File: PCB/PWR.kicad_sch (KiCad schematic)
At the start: 8 parts, among them U1 STPMIC1APQR

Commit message: PCB_Update
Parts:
- removed C1: 4.7uF, Capacitor_SMD:C_0402_1005Metric, symbol Device:C
- added C10, C11, C12, C13, C14, C15, C17: 10uF, Capacitor_SMD:C_0603_1608Metric, symbol Device:C
- added C16, C8, C9: 1uF, Capacitor_SMD:C_0402_1005Metric, symbol Device:C
- added C18: 4.7uF, Capacitor_SMD:C_0603_1608Metric, symbol Device:C
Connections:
- net at U1.12 (BUCK2IN): now also C11.2
- net at U1.13 (LDO3IN): now also C14.2
- net at U1.14 (LDO3OUT): now also C15.1
- net at U1.16 (VREFDDR): now also C16.1
- net at U1.19 (LDO25IN): now also C9.2
- net at U1.22 (LDO16IN): now also C8.2
- net at U1.24 (BUCK4IN): now also C13.2
- net at U1.28 (BUCK3IN): now also C12.2
- net at U1.35 (VBUSOTG): now also C18.1
- net at U1.8 (BUCK1IN): now also C10.2
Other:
- note removed: "CVIN, CLDO1OUT, CLDO2OUT, CLDO4OUT, CLDO5OUT, CLDO6OUT, CINTLDO"
- moved on the sheet: C2, C3, C4, C5, C6, C7, U1

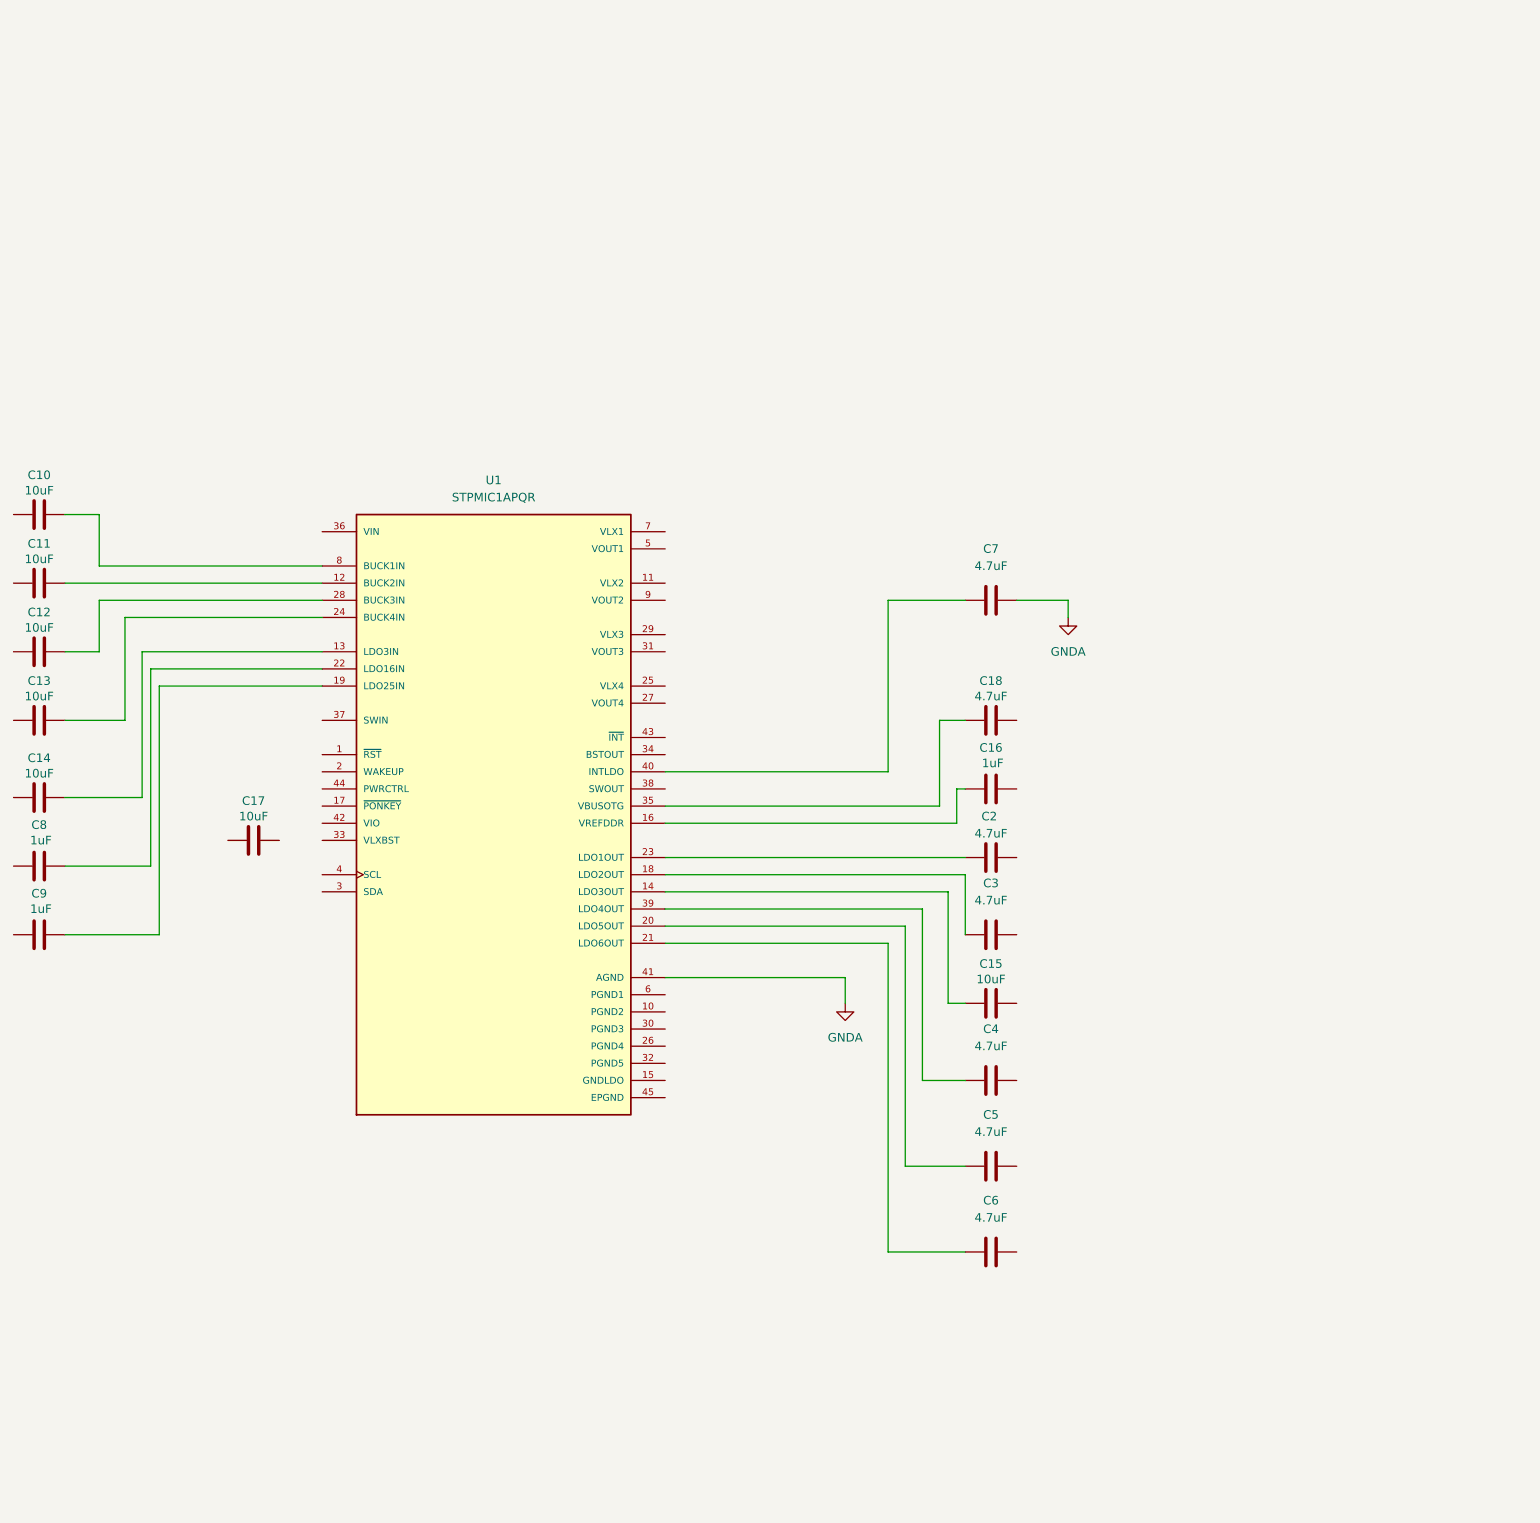
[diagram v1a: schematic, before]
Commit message: PCB_UPDATE. PWR DONE, DDR STARTED
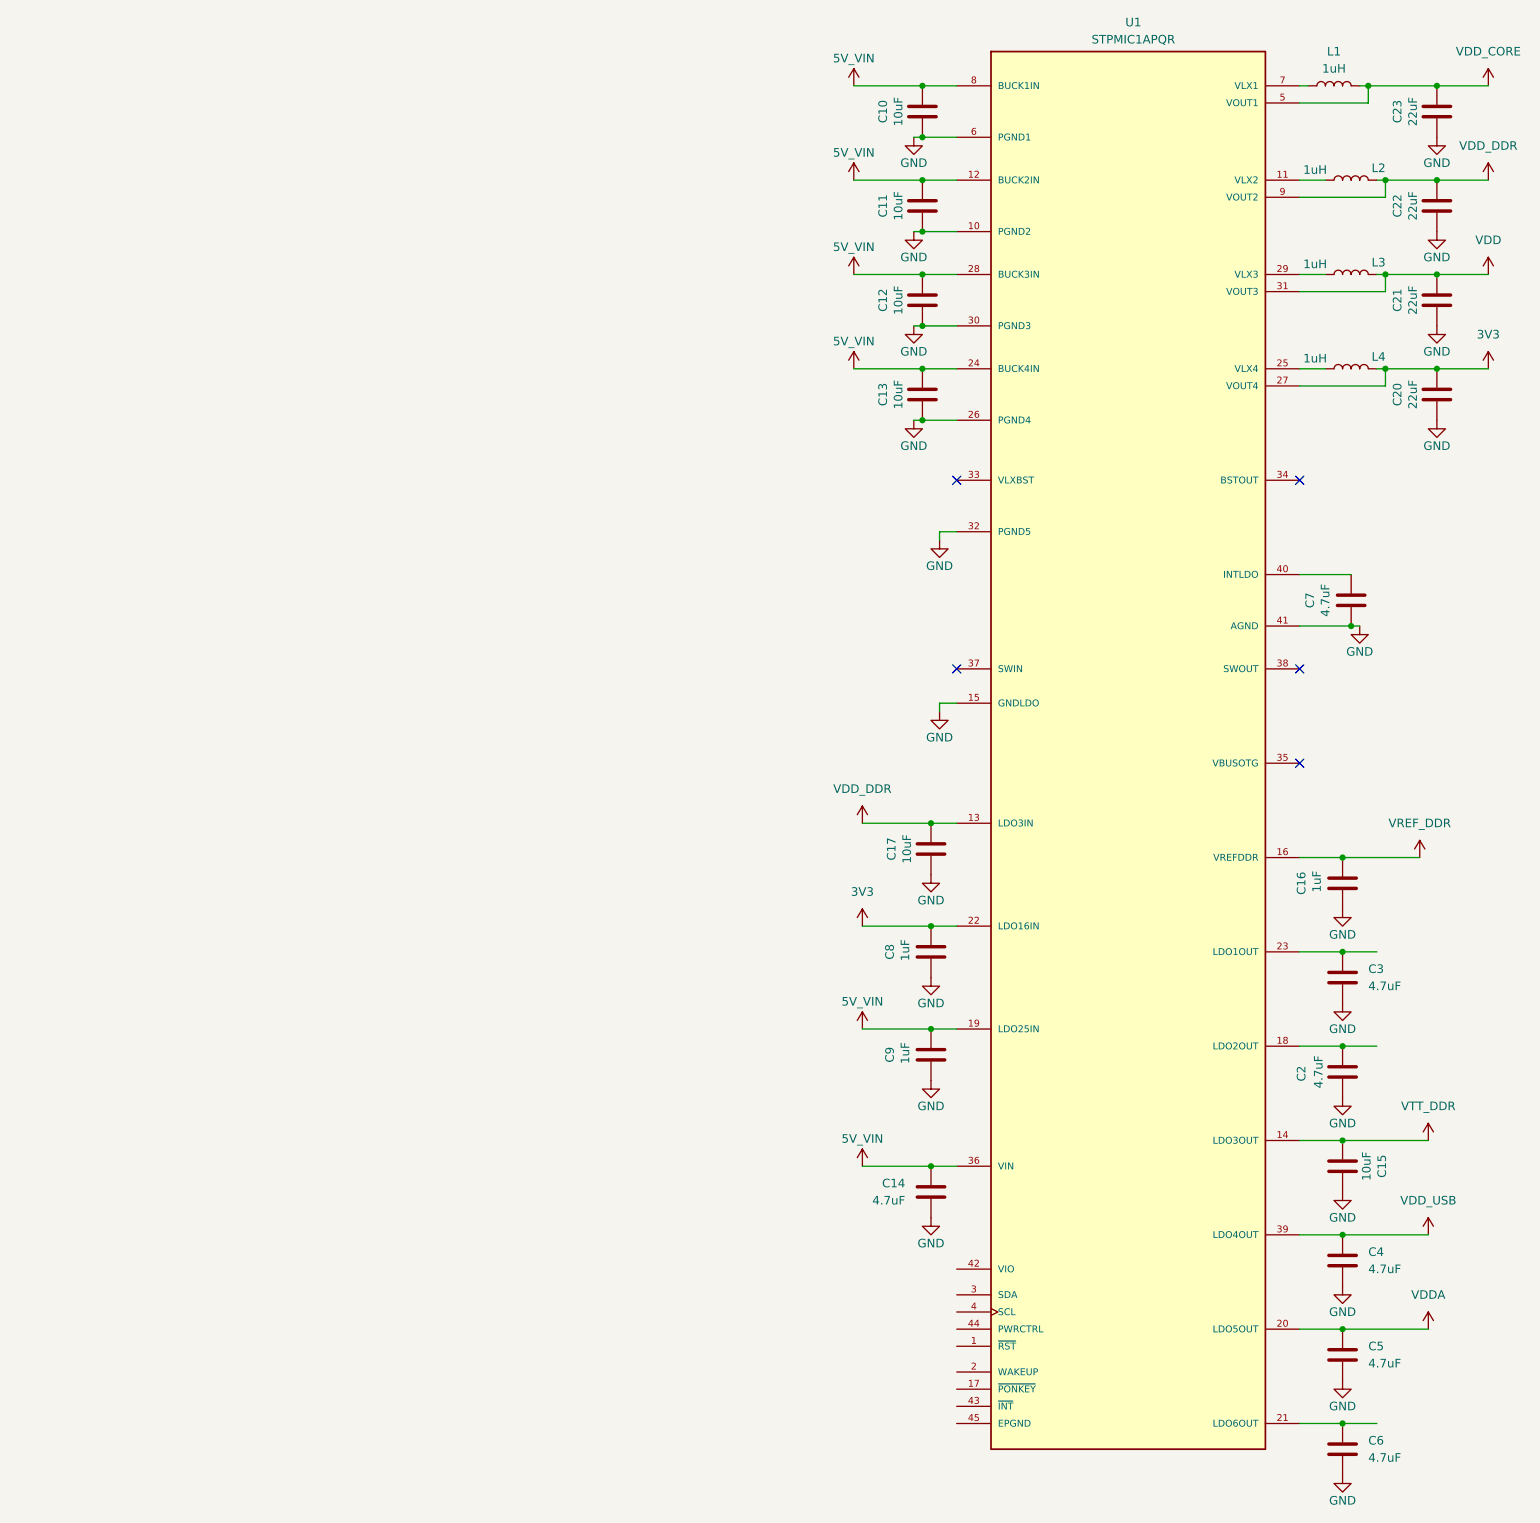
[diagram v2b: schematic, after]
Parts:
- removed C18: 4.7uF, Capacitor_SMD:C_0603_1608Metric, symbol Device:C
- added C20, C21, C22, C23: 22uF, Capacitor_SMD:C_0603_1608Metric, symbol Device:C
- added L1, L2, L3, L4: 1uH, Inductor_SMD:L_1008_2520Metric, symbol Device:L
- C14: value 10uF -> 4.7uF; footprint Capacitor_SMD:C_0603_1608Metric -> Capacitor_SMD:C_0402_1005Metric; Mouser P/N 81-GRT188R61A106KE3D -> 81-GRM155R60J475ME7J; P/N GRT188R61A106KE13D -> GRM155R60J475ME47
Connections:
- net GND: now reaches C11.1
- net GND: now also C10.1, C12.1, C13.1, C14.1, C15.2, C16.1, C17.1, C2.1, C3.1, C4.1, C5.1, C6.1, C7.1, C8.1, C9.1, U1.10 (PGND2), U1.15 (GNDLDO), U1.26 (PGND4), U1.30 (PGND3), U1.32 (PGND5), U1.41 (AGND), U1.6 (PGND1), C20.1, C21.1, C22.1, C23.1
- net 5V_VIN: now reaches C11.2, U1.12 (BUCK2IN)
- net 5V_VIN: now also C10.2, C12.2, C13.2, C14.2, C9.2, U1.19 (LDO25IN), U1.24 (BUCK4IN), U1.28 (BUCK3IN), U1.36 (VIN), U1.8 (BUCK1IN)
- net at U1.11 (VLX2): now also L2.1
- net VDD_DDR: now reaches U1.13 (LDO3IN)
- net VDD_DDR: now also C17.2, U1.9 (VOUT2), C22.2, L2.2; no longer C14.2
- net VTT_DDR: now reaches C15.1, U1.14 (LDO3OUT)
- net VREF_DDR: now reaches U1.16 (VREFDDR)
- net VREF_DDR: now also C16.2; no longer C16.1
- net at U1.18 (LDO2OUT): now also C2.2; no longer C3.1
- net VDDA: now reaches U1.20 (LDO5OUT)
- net VDDA: now also C5.2; no longer C5.1
- net at U1.21 (LDO6OUT): now also C6.2; no longer C6.1
- net 3V3: now reaches C8.2, U1.22 (LDO16IN)
- net 3V3: now also U1.27 (VOUT4), C20.2, L4.2
- net at U1.23 (LDO1OUT): now also C3.2; no longer C2.1
- net at U1.25 (VLX4): now also L4.1
- net at U1.29 (VLX3): now also L3.1
- net VDD: now reaches U1.31 (VOUT3)
- net VDD: now also C21.2, L3.2
- net VDD_USB: now reaches U1.39 (LDO4OUT)
- net VDD_USB: now also C4.2; no longer C4.1
- net at U1.40 (INTLDO): now also C7.2; no longer C7.1
- net VDD_CORE: now reaches U1.5 (VOUT1)
- net VDD_CORE: now also C23.2, L1.2
- net at U1.7 (VLX1): now also L1.1
- removed net GNDA: C7.2, U1.41 (AGND)
- no-connect marks 0 -> 5
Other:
- moved on the sheet: C10, C11, C12, C13, C15, C16, C17, C2, C3, C4, C5, C6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

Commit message: PCB_UPDATE
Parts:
- added R40: 0, symbol Device:R
- U1: Availability In Stock -> (none); Check_prices https://www.snapeda.com/parts/STPMIC1APQR/STMicroelectronic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 -> (none); Description_1 General Purpose PMIC 44-WFQFN (5x6) -> (none); MANUFACTURER STMicroelectronics -> (none); MAXIMUM_PACKAGE_HEIGHT 0.8mm -> (none); MF STMicroelectronics -> (none); MP STPMIC1APQR -> (none); Mouser P/N (none) -> 511-STPMIC1APQR; P/N (none) -> STPMIC1APQR; PARTREV 8 -> (none); Package WFQFN-44 STMicroelectronics -> (none); Price None -> (none); STANDARD IPC 7351B -> (none); SnapEDA_Link https://www.snapeda.com/parts/STPMIC1APQR/STMicroelectronic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 -> (none)
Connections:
- net at U1.1 (~{RST}): now also R40.1
- net PWR_ON: now reaches U1.44 (PWRCTRL)
- new net NRST: R40.2
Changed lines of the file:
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@@
 	(wire
 		(pts
+			(xy 280.67 222.25) (xy 285.75 222.25)
+		)
+		(stroke
+			(width 0)
+			(type default)
+		)
+	)
+	(wire
+		(pts
 			(xy 303.53 85.09) (xy 304.8 85.09)
 		)
@@
 	(wire
 		(pts
+			(xy 293.37 222.25) (xy 309.88 222.25)
+		)
+		(stroke
+			(width 0)
+			(type default)
+		)
+	)
+	(wire
+		(pts
 			(xy 373.38 77.47) (xy 373.38 80.01)
 		)
@@
 		)
 	)
+	(global_label "NRST"
+		(shape input)
+		(at 280.67 222.25 180)
+		(fields_autoplaced yes)
+		(effects
+			(font
+				(size 1.27 1.27)
+			)
+			(justify right)
+		)
+		(property "Intersheetrefs" "${INTERSHEET_REFS}"
+			(at 272.9072 222.25 0)
+			(effects
+				(font
+					(size 1.27 1.27)
+				)
+				(justify right)
+				(hide yes)
+			)
+		)
+	)
+	(global_label "PWR_ON"
+		(shape input)
+		(at 309.88 219.71 180)
+		(fields_autoplaced yes)
+		(effects
+			(font
+				(size 1.27 1.27)
+			)
+			(justify right)
+		)
+		(property "Intersheetrefs" "${INTERSHEET_REFS}"
+			(at 299.2748 219.71 0)
+			(effects
+				(font
+					(size 1.27 1.27)
+				)
+				(justify right)
+				(hide yes)
+			)
+		)
+	)
 	(symbol
 		(lib_id "power:GND")
@@
 			)
 		)
-		(property "MF" "STMicroelectronics"
-			(at 335.28 105.41 0)
-			(effects
-				(font
-					(size 1.27 1.27)
-				)
-				(justify bottom)
-				(hide yes)
-			)
-		)
-		(property "MAXIMUM_PACKAGE_HEIGHT" "0.8mm"
-			(at 335.28 105.41 0)
-			(effects
-				(font
-					(size 1.27 1.27)
-				)
-				(justify bottom)
-				(hide yes)
-			)
-		)
-		(property "Package" "WFQFN-44 STMicroelectronics"
-			(at 335.28 105.41 0)
-			(effects
-				(font
-					(size 1.27 1.27)
-				)
-				(justify bottom)
-				(hide yes)
-			)
-		)
-		(property "Price" "None"
-			(at 335.28 105.41 0)
-			(effects
-				(font
-					(size 1.27 1.27)
-				)
-				(justify bottom)
-				(hide yes)
-			)
-		)
-		(property "Check_prices" "https://www.snapeda.com/parts/STPMIC1APQR/STMicroelectronics/view-part/?ref=eda"
-			(at 335.28 132.08 0)
-			(effects
-				(font
-					(size 1.27 1.27)
-				)
-				(justify bottom)
-				(hide yes)
-			)
-		)
-		(property "STANDARD" "IPC 7351B"
-			(at 335.28 105.41 0)
-			(effects
-				(font
-					(size 1.27 1.27)
-				)
-				(justify bottom)
-				(hide yes)
-			)
-		)
-		(property "PARTREV" "8"
-			(at 335.28 105.41 0)
-			(effects
-				(font
-					(size 1.27 1.27)
-				)
-				(justify bottom)
-				(hide yes)
-			)
-		)
-		(property "SnapEDA_Link" "https://www.snapeda.com/parts/STPMIC1APQR/STMicroelectronics/view-part/?ref=snap"
-			(at 335.28 132.08 0)
-			(effects
-				(font
-					(size 1.27 1.27)
-				)
-				(justify bottom)
-				(hide yes)
-			)
-		)
-		(property "MP" "STPMIC1APQR"
-			(at 335.28 105.41 0)
-			(effects
-				(font
-					(size 1.27 1.27)
-				)
-				(justify bottom)
-				(hide yes)
-			)
-		)
-		(property "Description_1" "General Purpose PMIC 44-WFQFN (5x6)"
-			(at 335.28 105.41 0)
-			(effects
-				(font
-					(size 1.27 1.27)
-				)
-				(justify bottom)
-				(hide yes)
-			)
-		)
-		(property "Availability" "In Stock"
+		(property "Mouser P/N" "511-STPMIC1APQR"
 			(at 335.28 105.41 0)
 			(effects
@@
 					(size 1.27 1.27)
 				)
-				(justify bottom)
 				(hide yes)
 			)
 		)
-		(property "MANUFACTURER" "STMicroelectronics"
+		(property "P/N" "STPMIC1APQR "
 			(at 335.28 105.41 0)
 			(effects
@@
 					(size 1.27 1.27)
 				)
-				(justify bottom)
 				(hide yes)
 			)
@@
 					(unit 1)
 				)
+			)
+		)
+	)
+	(symbol
+		(lib_id "Device:R")
+		(at 289.56 222.25 270)
+		(unit 1)
+		(exclude_from_sim no)
+		(in_bom yes)
+		(on_board yes)
+		(dnp no)
+		(property "Reference" "R40"
+			(at 284.988 220.726 90)
+			(effects
+				(font
+					(size 1.27 1.27)
+				)
+			)
+		)
+		(property "Value" "0"
+			(at 294.132 220.472 90)
+			(effects
+				(font
+					(size 1.27 1.27)
+				)
+			)
+		)
+		(property "Footprint" ""
+			(at 289.56 220.472 90)
+			(effects
+				(font
+					(size 1.27 1.27)
+				)
+				(hide yes)
+			)
+		)
+		(property "Datasheet" "~"
+			(at 289.56 222.25 0)
+			(effects
+				(font
+					(size 1.27 1.27)
+				)
+				(hide yes)
+			)
+		)
+		(property "Description" "Resistor"
+			(at 289.56 222.25 0)
+			(effects
+				(font
+					(size 1.27 1.27)
+				)
+				(hide yes)
+			)
+		)
+		(property "Mouser P/N" ""
+			(at 289.56 222.25 0)
+			(effects
+				(font
+					(size 1.27 1.27)
+				)
+				(hide yes)
+			)
+		)
+		(pin "1"
+		)
+		(pin "2"
+		)
+		(instances
+			(project "MPU_MOD"
+				(path "/65890f61-d586-475b-928a-b635a5e4e59e/355c85ef-822d-4607-91cf-41bd60068331"
+					(reference "R40")
+					(unit 1)
+				)

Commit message: PCB_UPDATE
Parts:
- added U9: STC3115IQT, STC3115IQT:SON50P300X200X60-10N, symbol STC3115IQT:STC3115IQT
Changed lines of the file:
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@@
+	)
+	(symbol
+		(lib_id "STC3115IQT:STC3115IQT")
+		(at 205.74 62.23 0)
+		(unit 1)
+		(exclude_from_sim no)
+		(in_bom yes)
+		(on_board yes)
+		(dnp no)
+		(fields_autoplaced yes)
+		(property "Reference" "U9"
+			(at 205.74 44.45 0)
+			(effects
+				(font
+					(size 1.27 1.27)
+				)
+			)
+		)
+		(property "Value" "STC3115IQT"
+			(at 205.74 46.99 0)
+			(effects
+				(font
+					(size 1.27 1.27)
+				)
+			)
+		)
+		(property "Footprint" "STC3115IQT:SON50P300X200X60-10N"
+			(at 205.74 62.23 0)
+			(effects
+				(font
+					(size 1.27 1.27)
+				)
+				(justify bottom)
+				(hide yes)
+			)
+		)
+		(property "Datasheet" ""
+			(at 205.74 62.23 0)
+			(effects
+				(font
+					(size 1.27 1.27)
+				)
+				(hide yes)
+			)
+		)
+		(property "Description" ""
+			(at 205.74 62.23 0)
+			(effects
+				(font
+					(size 1.27 1.27)
+				)
+				(hide yes)
+			)
+		)
+		(property "MF" "STMicroelectronics"
+			(at 205.74 62.23 0)
+			(effects
+				(font
+					(size 1.27 1.27)
+				)
+				(justify bottom)
+				(hide yes)
+			)
+		)
+		(property "Description_1" "Battery Battery Monitor IC - 10-DFN (3x2)"
+			(at 205.74 62.23 0)
+			(effects
+				(font
+					(size 1.27 1.27)
+				)
+				(justify bottom)
+				(hide yes)
+			)
+		)
+		(property "Package" "DFN-10 STMicroelectronics"
+			(at 205.74 62.23 0)
+			(effects
+				(font
+					(size 1.27 1.27)
+				)
+				(justify bottom)
+				(hide yes)
+			)
+		)
+		(property "Price" "None"
+			(at 205.74 62.23 0)
+			(effects
+				(font
+					(size 1.27 1.27)
+				)
+				(justify bottom)
+				(hide yes)
+			)
+		)
+		(property "Check_prices" "https://www.snapeda.com/parts/STC3115IQT/STMicroelectronics/view-part/?ref=eda"
+			(at 205.74 62.23 0)
+			(effects
+				(font
+					(size 1.27 1.27)
+				)
+				(justify bottom)
+				(hide yes)
+			)
+		)
+		(property "STANDARD" "IPC 7351B"
+			(at 205.74 62.23 0)
+			(effects
+				(font
+					(size 1.27 1.27)
+				)
+				(justify bottom)
+				(hide yes)
+			)
+		)
+		(property "PARTREV" "9"
+			(at 205.74 62.23 0)
+			(effects
+				(font
+					(size 1.27 1.27)
+				)
+				(justify bottom)
+				(hide yes)
+			)
+		)
+		(property "SnapEDA_Link" "https://www.snapeda.com/parts/STC3115IQT/STMicroelectronics/view-part/?ref=snap"
+			(at 205.74 62.23 0)
+			(effects
+				(font
+					(size 1.27 1.27)
+				)
+				(justify bottom)
+				(hide yes)
+			)
+		)
+		(property "MP" "STC3115IQT"
+			(at 205.74 62.23 0)
+			(effects
+				(font
+					(size 1.27 1.27)
+				)
+				(justify bottom)
+				(hide yes)
+			)
+		)
+		(property "Availability" "In Stock"
+			(at 205.74 62.23 0)
+			(effects
+				(font
+					(size 1.27 1.27)
+				)
+				(justify bottom)
+				(hide yes)
+			)
+		)
+		(property "MANUFACTURER" "ST MICROELECTRONICS"
+			(at 205.74 62.23 0)
+			(effects
+				(font
+					(size 1.27 1.27)
+				)
+				(justify bottom)
+				(hide yes)
+			)
+		)
+		(pin "7"
+		)
+		(pin "1"
+		)
+		(pin "9"
+		)
+		(pin "6"
+		)
+		(pin "10"
+		)
+		(pin "3"
+		)
+		(pin "2"
+		)
+		(pin "8"
+		)
+		(pin "5"
+		)
+		(instances
+			(project ""
+				(path "/65890f61-d586-475b-928a-b635a5e4e59e/355c85ef-822d-4607-91cf-41bd60068331"
+					(reference "U9")
+					(unit 1)
+				)
+			)
+		)
 	)
 	(symbol
